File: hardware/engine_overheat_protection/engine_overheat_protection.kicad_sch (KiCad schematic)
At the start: 9 parts, among them SW1 SW_Push, SW2 SW_SPST

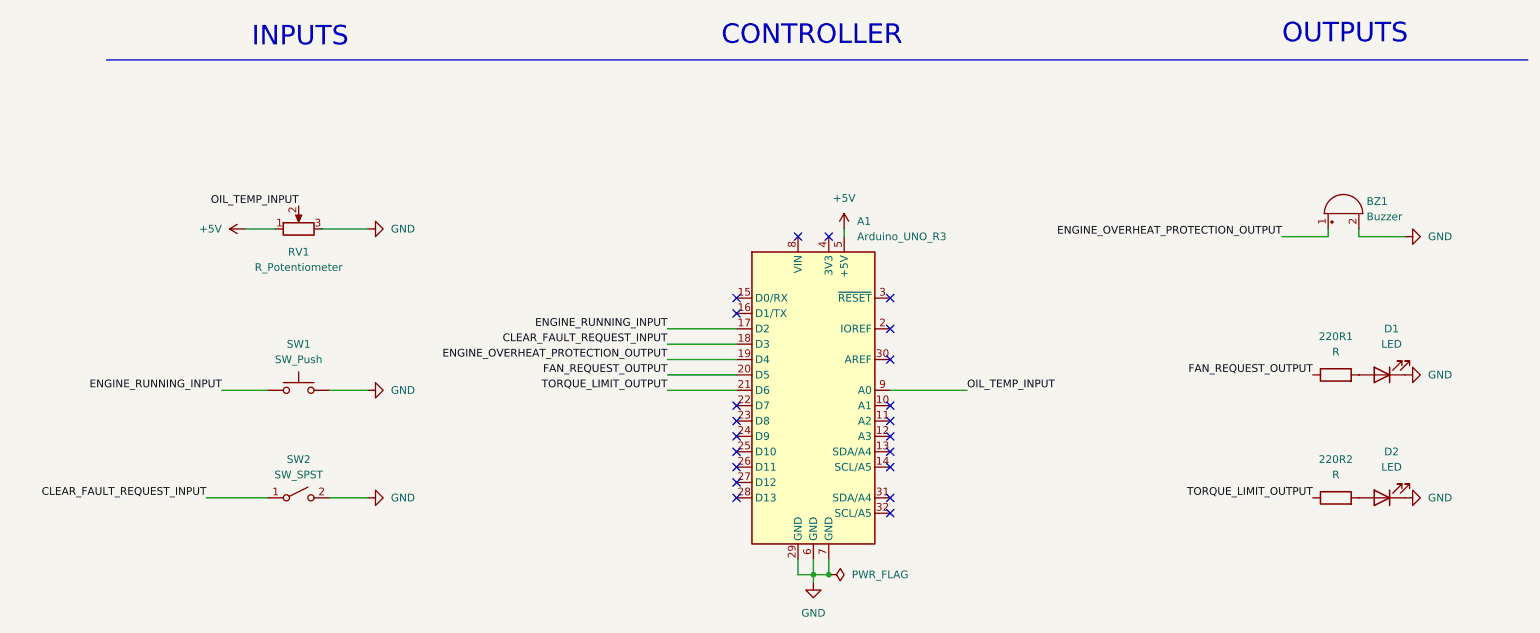
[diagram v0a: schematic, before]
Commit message: docs: add fault output pin to engine overheat protection hardware circuit
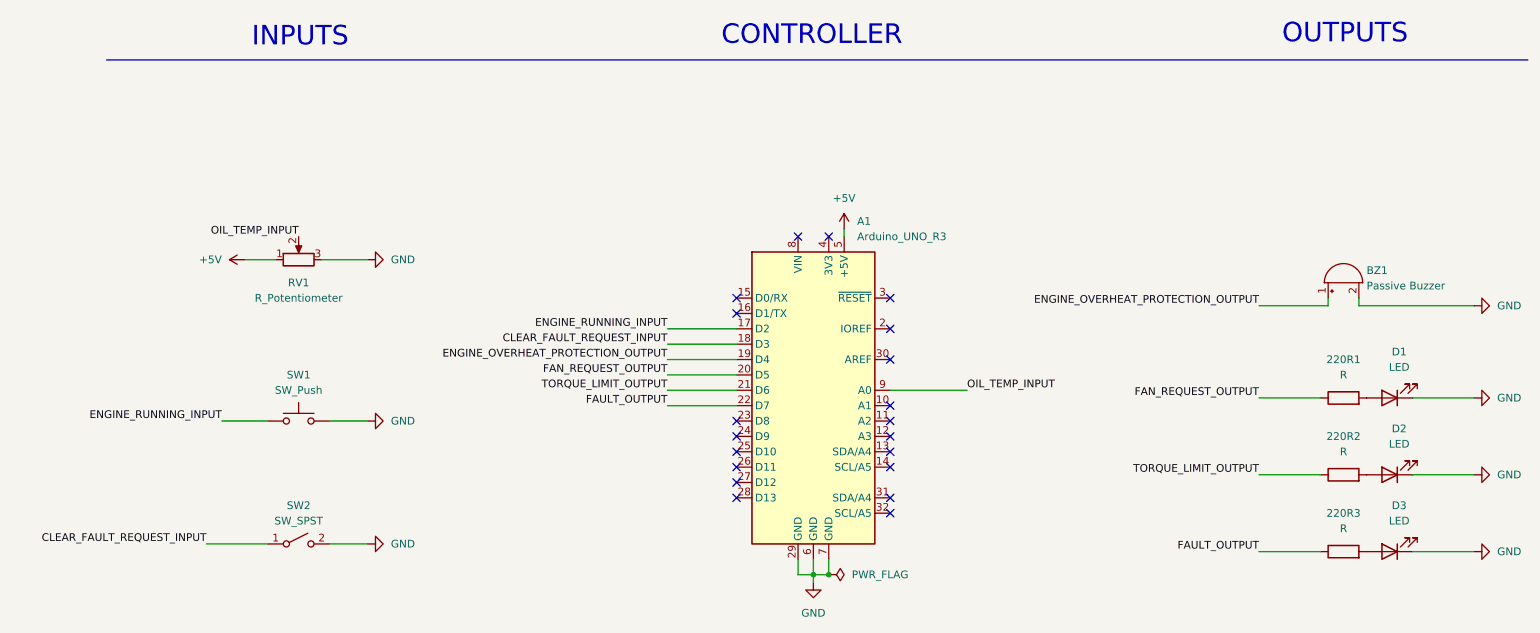
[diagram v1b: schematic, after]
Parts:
- added 220R3: R, symbol Device:R
- added D3: LED, symbol Device:LED
- BZ1: value Buzzer -> Passive Buzzer
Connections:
- net GND: now also D3.1 (K)
- net FAULT_OUTPUT: now reaches A1.22 (D7)
- net FAULT_OUTPUT: now also 220R3.1
- new net: 220R3.2, D3.2 (A)
- no-connect marks 21 -> 20
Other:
- moved on the sheet: 220R1, 220R2, BZ1, D1, D2, RV1, SW1, SW2
